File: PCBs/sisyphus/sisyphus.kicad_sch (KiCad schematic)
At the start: 31 parts, among them J4 USB_BOOT, J7 SWD, U4 W25Q128JVS, U7 RP2040, Y1 ABM8-272-T3

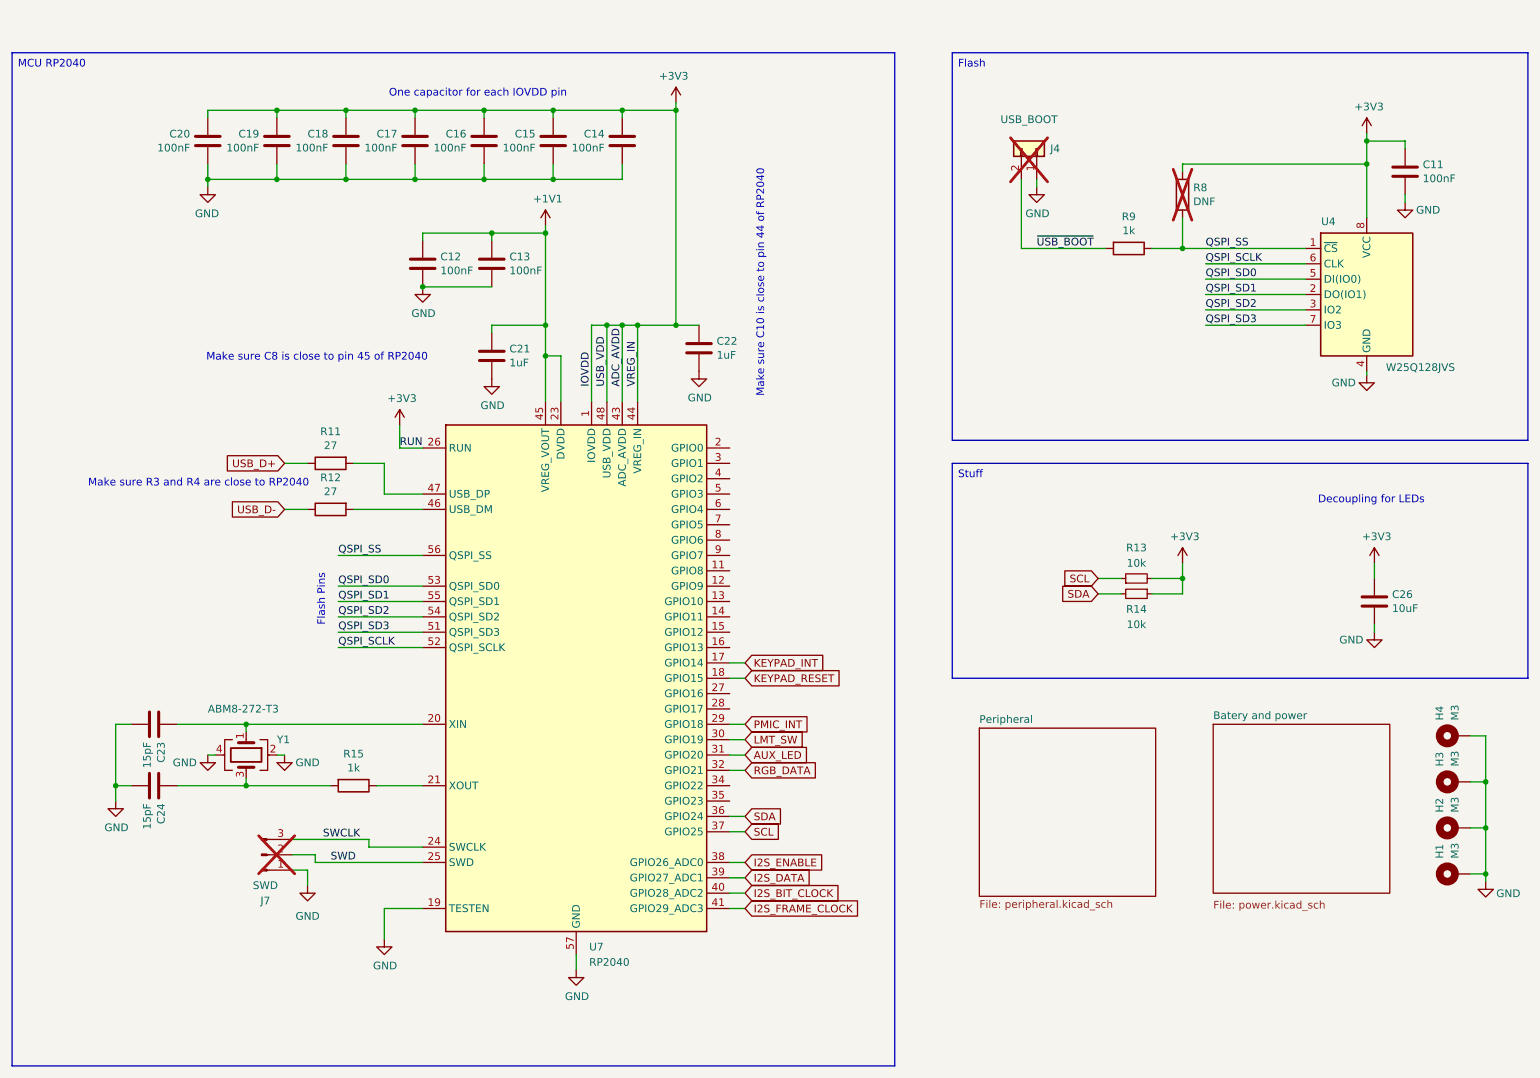
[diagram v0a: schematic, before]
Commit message: Fix things on PCB, update inductor size
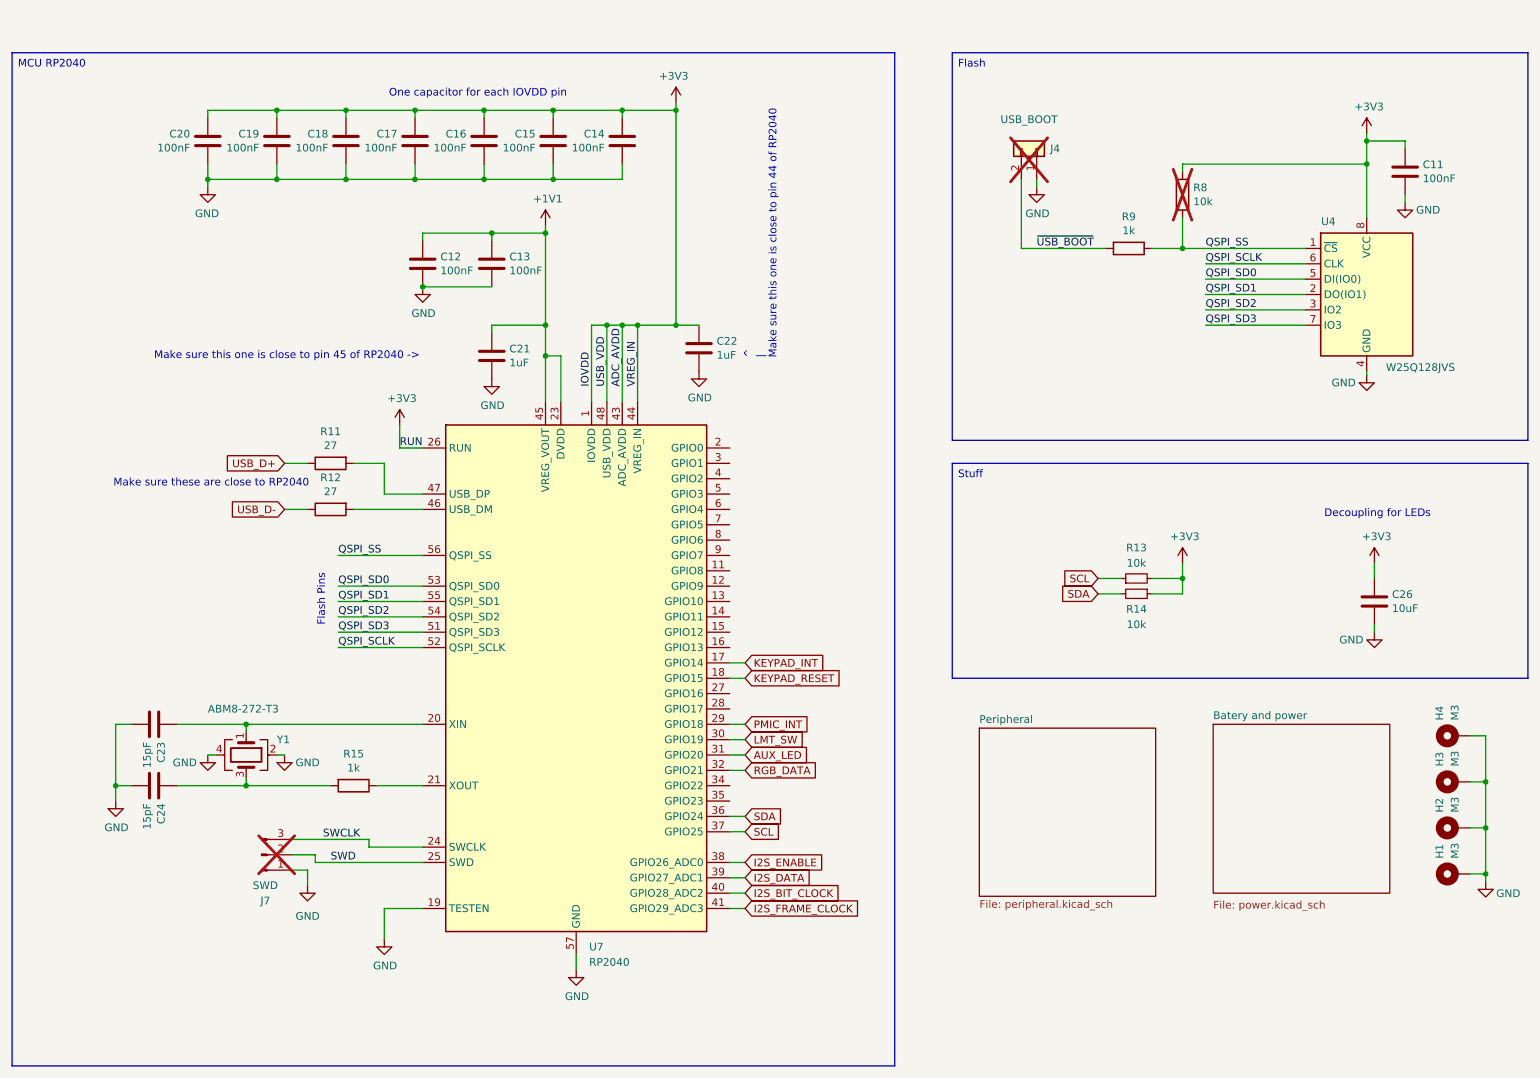
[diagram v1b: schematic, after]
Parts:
- R8: value DNF -> 10k
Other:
- note added: "Make sure these are close to RP2040"
- note added: "Make sure this one is close to pin 45 of RP2040 ->"
- note added: "^ | Make sure this one is close to pin 44 of RP2040"
- note removed: "Make sure C10 is close to pin 44 of RP2040"
- note removed: "Make sure C8 is close to pin 45 of RP2040"
- note removed: "Make sure R3 and R4 are close to RP2040"
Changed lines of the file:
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@@
 		(company "Plajta corp.")
 	)
-	(text "Make sure C8 is close to pin 45 of RP2040"
+	(text "Make sure this one is close to pin 45 of RP2040 ->"
 		(exclude_from_sim no)
-		(at 54.356 70.866 0)
+		(at 45.72 70.612 0)
 		(effects
 			(font
@@
 	(text "Decoupling for LEDs"
 		(exclude_from_sim no)
-		(at 247.142 93.726 0)
-		(effects
-			(font
-				(size 1.27 1.27)
-			)
-		)
-	)
-	(text "Make sure R3 and R4 are close to RP2040"
+		(at 248.158 96.012 0)
+		(effects
+			(font
+				(size 1.27 1.27)
+			)
+		)
+	)
+	(text "Make sure these are close to RP2040"
 		(exclude_from_sim no)
 		(at 71.374 91.694 0)
@@
 		)
 	)
-	(text "Make sure C10 is close to pin 44 of RP2040"
+	(text "^\n|\nMake sure this one is close to pin 44 of RP2040"
 		(exclude_from_sim no)
-		(at 146.812 76.708 90)
+		(at 148.844 70.358 90)
 		(effects
 			(font
@@
 			)
 		)
-		(property "Value" "DNF"
+		(property "Value" "10k"
 			(at 217.678 44.323 0)
 			(effects

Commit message: Add the first actually ordered version of the PCB
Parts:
- C14: renamed from C23; LCSC Part (none) -> https://lcsc.com/product-detail/Multilayer-Ceramic-Capacito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
- C15: renamed from C24; LCSC Part (none) -> https://lcsc.com/product-detail/Multilayer-Ceramic-Capacito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
- R3: renamed from R11; value 27 -> 33
- R4: renamed from R12; value 27 -> 33
- U1: renamed from U4; LCSC Part (none) -> https://lcsc.com/product-detail/NOR-FLASH_Winbond-Elec-W25Q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
- U2: renamed from U7; LCSC Part (none) -> https://lcsc.com/product-detail/Microcontrollers-MCU-MPU-SO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
- Y1: LCSC Part (none) -> https://lcsc.com/product-detail/Crystals_Abracon-LLC-ABM8-2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
- renumbered C20 to C1, C13 to C10, C22 to C11, C21 to C12, C26 to C13, C19 to C2, C18 to C3, C17 to C4, C16 to C5, C15 to C6, C14 to C7, C11 to C8, C12 to C9, H4 to H1, H3 to H2, H2 to H3, H1 to H4, J4 to J1, J7 to J2, R8 to R1, R9 to R2, R13 to R5, R14 to R6, R15 to R7
